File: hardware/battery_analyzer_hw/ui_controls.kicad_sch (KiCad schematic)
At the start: 10 parts, among them SW1 SW_Push, SW2 SW_Push, U3 ESP32-S3-WROOM-1

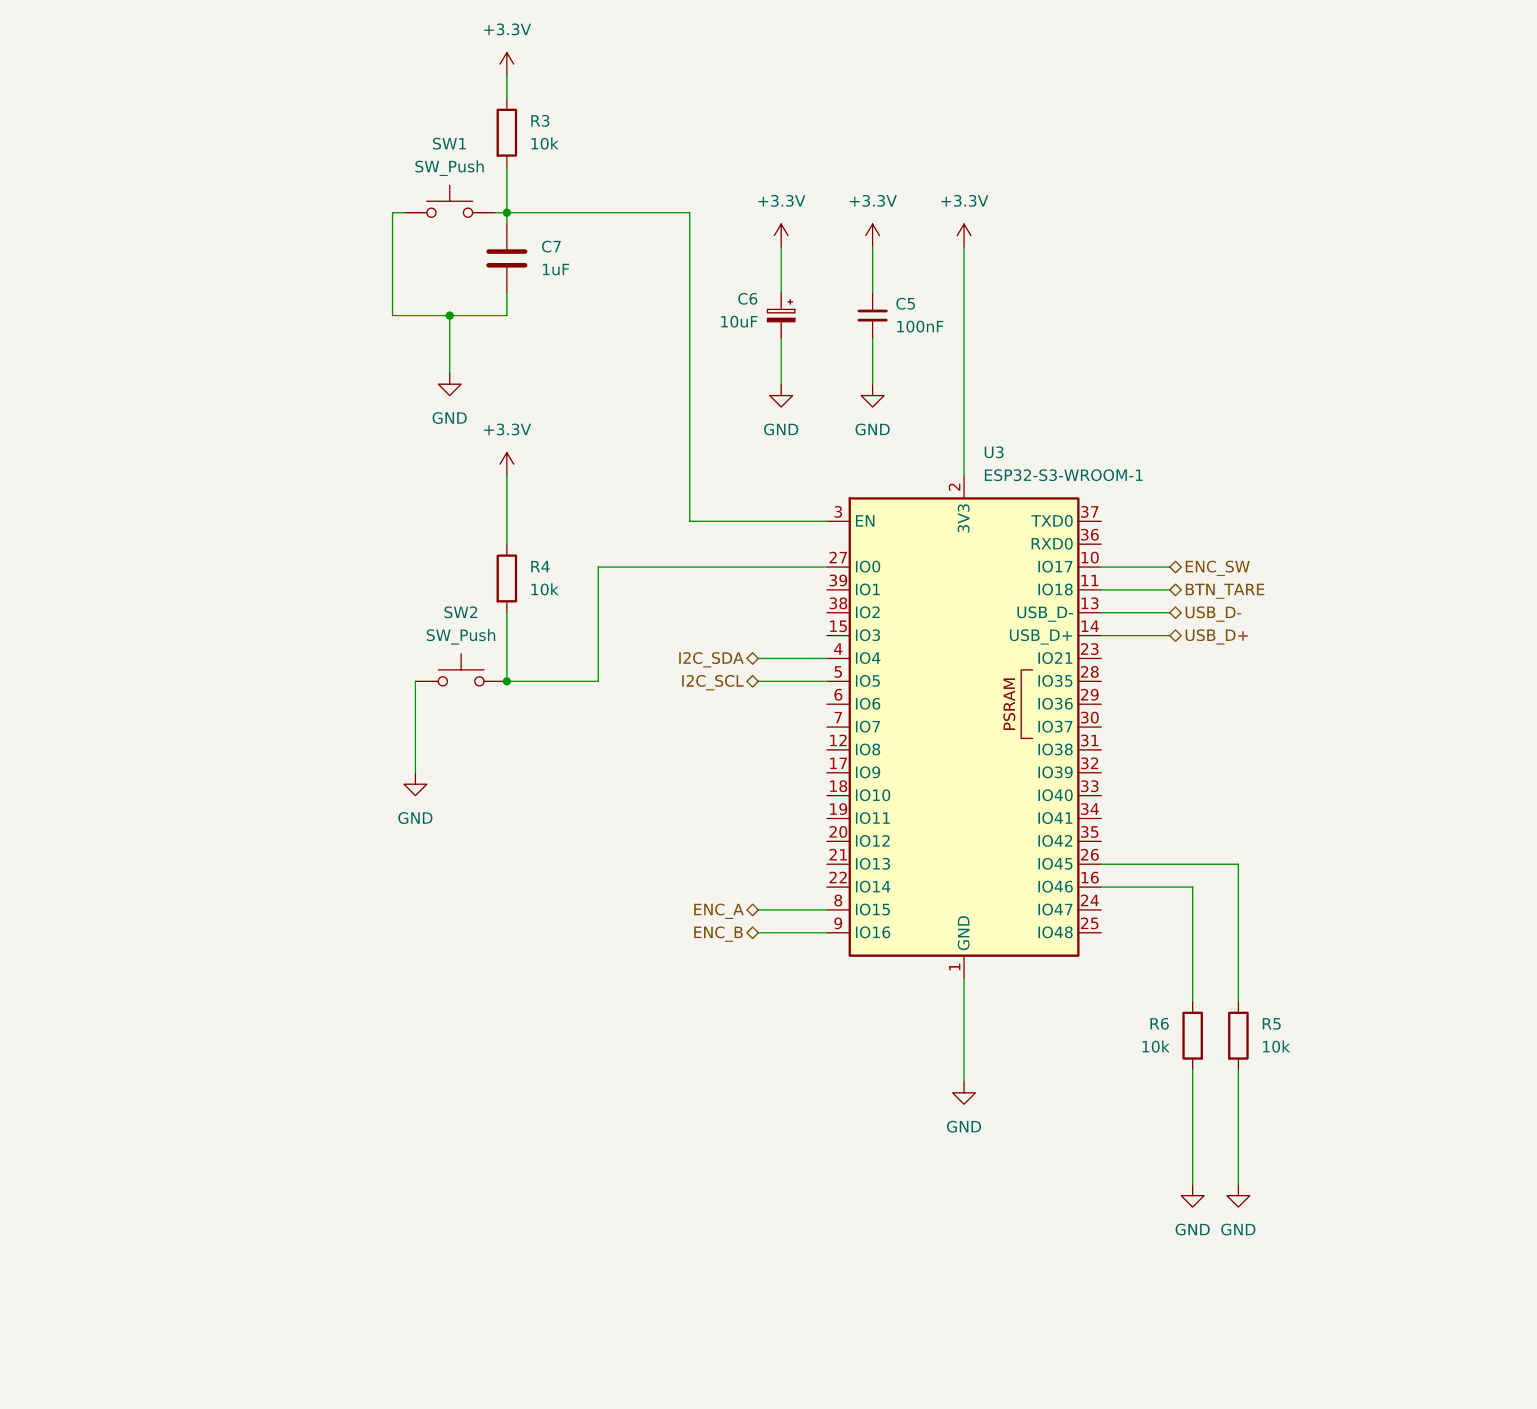
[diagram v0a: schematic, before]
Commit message: feat(hw): add UI sheet with dual OLEDs, encoder and button
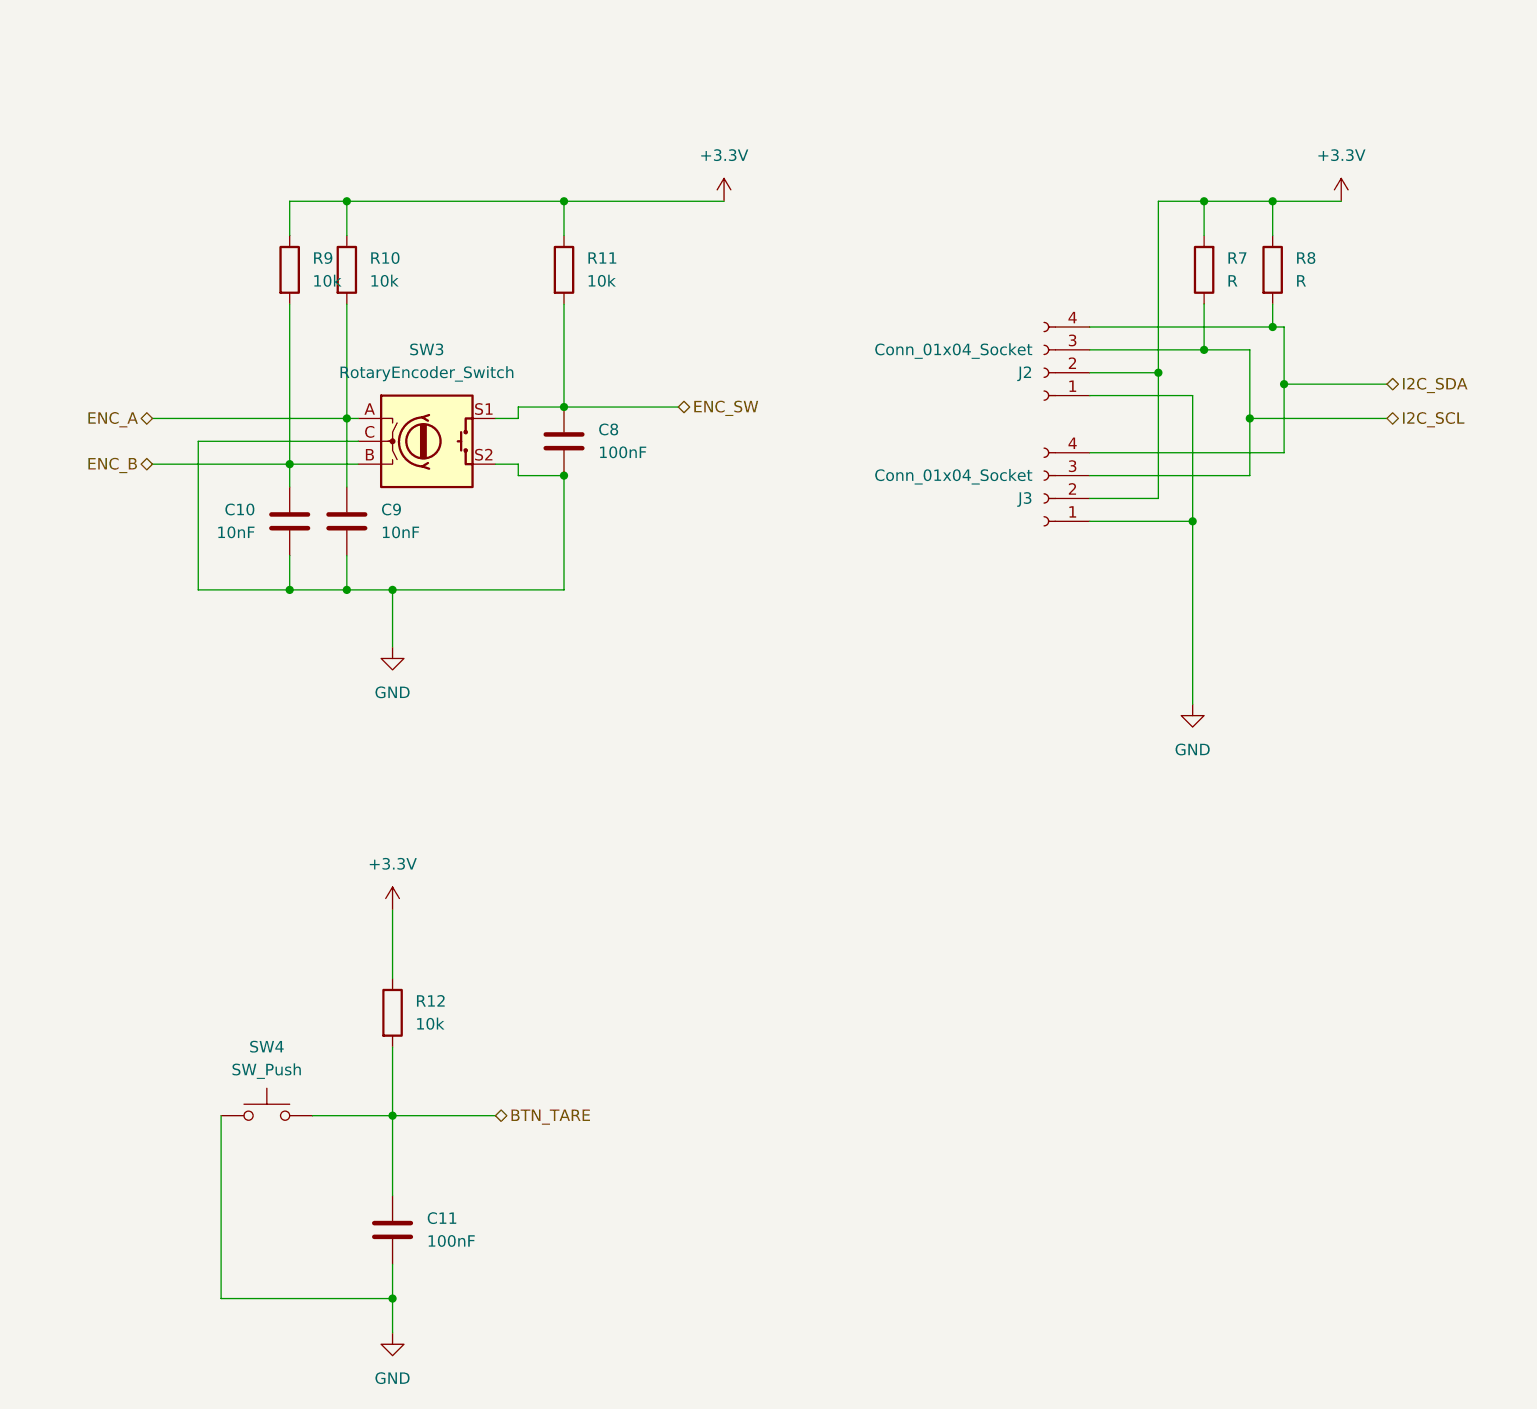
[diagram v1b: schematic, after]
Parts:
- removed C5: 100nF, Package_LCC:PLCC-44_16.6x16.6mm_P1.27mm, symbol Device:C_Small
- removed C6: 10uF, symbol Device:C_Polarized_Small
- removed C7: 1uF, symbol Device:C
- removed R3, R4, R5, R6: 10k, symbol Device:R
- removed SW1: SW_Push, symbol Switch:SW_Push
- removed SW2: SW_Push, Button_Switch_SMD:Nidec_Copal_CAS-120A, symbol Switch:SW_Push
- removed U3: ESP32-S3-WROOM-1, RF_Module:ESP32-S3-WROOM-1, symbol RF_Module:ESP32-S3-WROOM-1
- added C10, C9: 10nF, symbol Device:C
- added C11, C8: 100nF, symbol Device:C
- added J2, J3: Conn_01x04_Socket, symbol Connector:Conn_01x04_Socket
- added R10, R11, R12, R9: 10k, symbol Device:R
- added R7, R8: R, symbol Device:R
- added SW3: RotaryEncoder_Switch, symbol Device:RotaryEncoder_Switch
- added SW4: SW_Push, Button_Switch_SMD:Nidec_Copal_CAS-120A, symbol Switch:SW_Push
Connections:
- net +3.3V: now also J2.2 (Pin_2), J3.2 (Pin_2), R10.1, R11.1, R12.1, R7.2, R8.1, R9.1
- net BTN_TARE: now also C11.1, R12.2, SW4.2
- net ENC_A: now also C9.1, R10.2, SW3.A
- net ENC_B: now also C10.1, R9.2, SW3.B
- net ENC_SW: now also C8.1, R11.2, SW3.S1
- net GND: now also C10.2, C11.2, C8.2, C9.2, J2.1 (Pin_1), J3.1 (Pin_1), SW3.C, SW3.S2, SW4.1
- net I2C_SCL: now also J2.3 (Pin_3), J3.3 (Pin_3), R7.1
- net I2C_SDA: now also J2.4 (Pin_4), J3.4 (Pin_4), R8.2

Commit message: feat(hw): add RJ45 slave ports, isolated 1-Wire and PWM routing fix(hw): split I2C into UI and PWR buses to prevent PID blocking
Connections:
- net I2C_SCL renamed I2C_UI_SCL
- net I2C_SDA renamed I2C_UI_SDA
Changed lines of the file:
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@@
 		)
 	)
-	(hierarchical_label "I2C_SDA"
+	(hierarchical_label "I2C_UI_SDA"
 		(shape bidirectional)
 		(at 213.36 64.77 0)
@@
 		)
 	)
-	(hierarchical_label "I2C_SCL"
+	(hierarchical_label "I2C_UI_SCL"
 		(shape bidirectional)
 		(at 213.36 68.58 0)

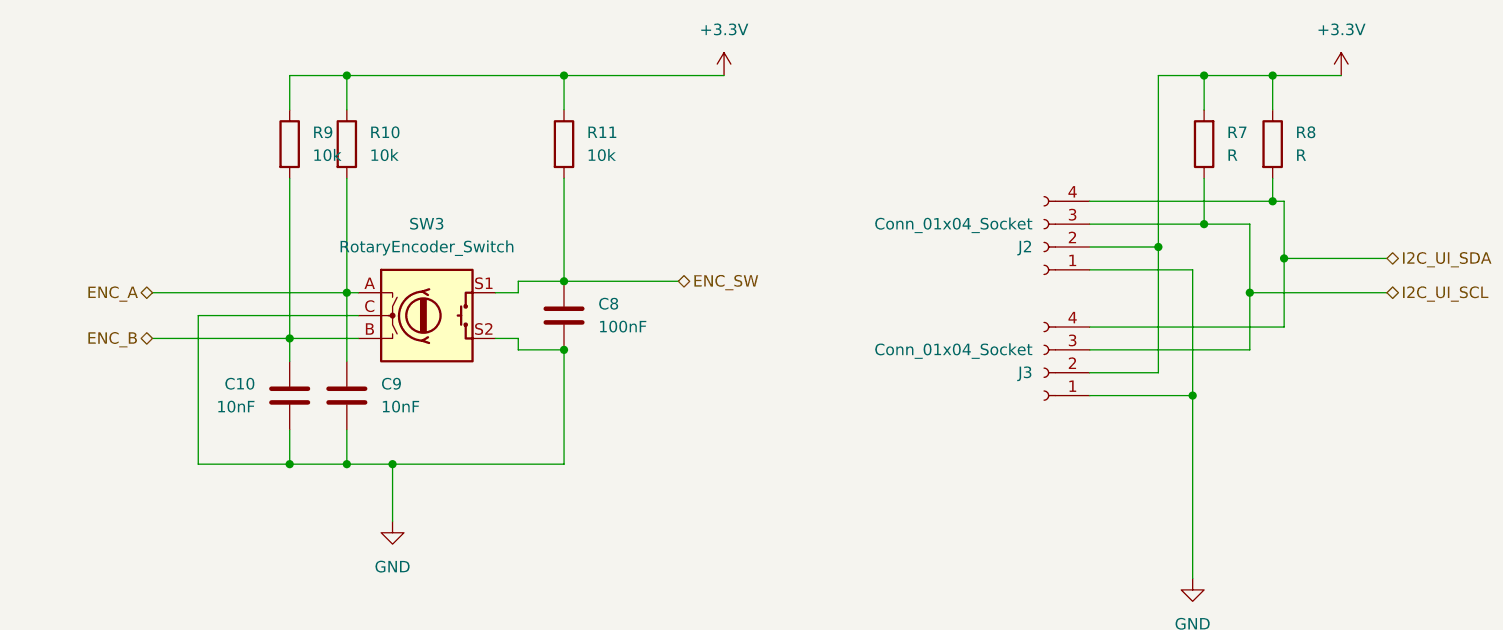
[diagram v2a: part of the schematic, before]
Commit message: hw(master): fix footprints, apply HandSolder and Tantalum
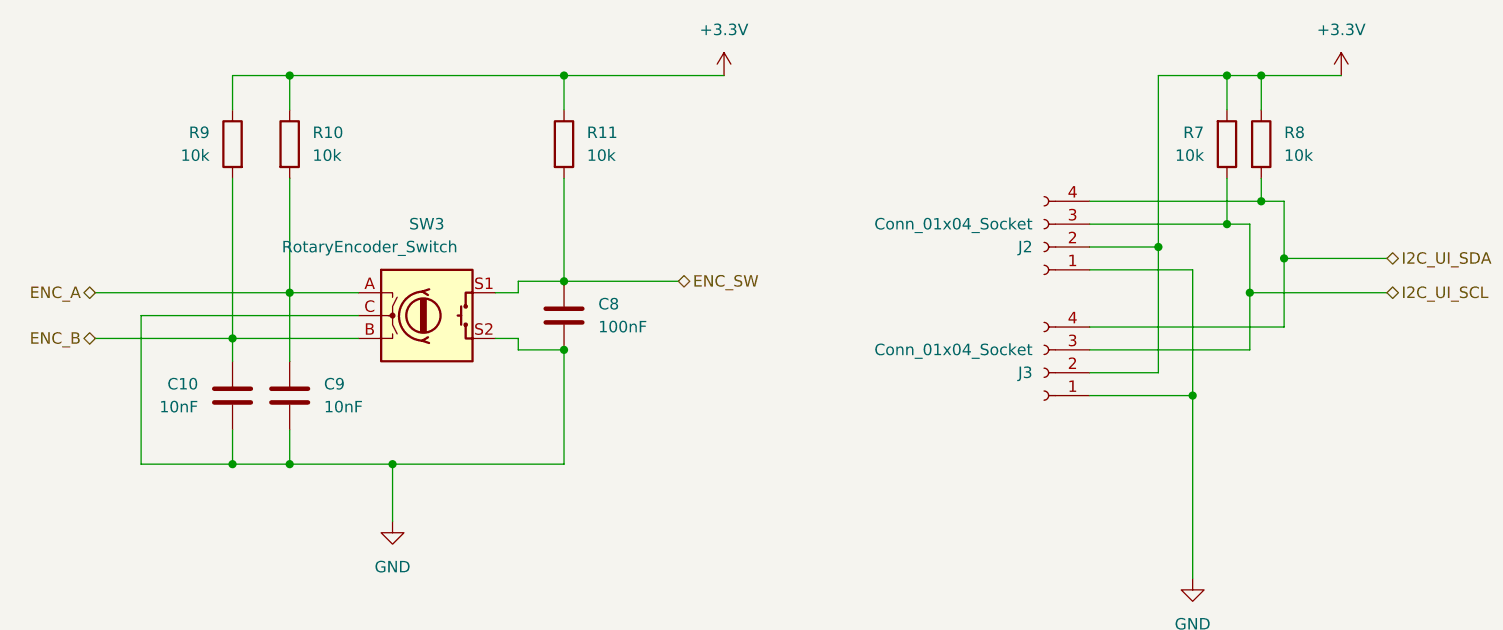
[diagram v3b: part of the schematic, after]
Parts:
- C10, C11, C8, C9: footprint (none) -> Capacitor_SMD:C_0805_2012Metric_Pad1.18x1.45mm_HandSolder
- J2, J3: footprint (none) -> Connector_PinHeader_2.54mm:PinHeader_1x04_P2.54mm_Vertical
- R10, R11, R12, R9: footprint (none) -> Resistor_SMD:R_0805_2012Metric_Pad1.20x1.40mm_HandSolder
- R7, R8: value R -> 10k; footprint (none) -> Resistor_SMD:R_0805_2012Metric_Pad1.20x1.40mm_HandSolder
- SW3: footprint (none) -> Rotary_Encoder:RotaryEncoder_Alps_EC12E-Switch_Vertical_H20mm
- SW4: footprint Button_Switch_SMD:Nidec_Copal_CAS-120A -> Button_Switch_THT:SW_PUSH_6mm
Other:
- moved on the sheet: C10, C9, R10, R7, R8, R9
